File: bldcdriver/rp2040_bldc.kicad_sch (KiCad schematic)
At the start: 12 parts, among them U2 RP2040

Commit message: Added the QSPI chip but not fully interfaced with the button/jumper, added decoupling capacitors for the RP2040
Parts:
- added C18: 100n, symbol Device:C_Small
- added U3: W25Q128JVS, Package_SO:SOIC-8_5.23x5.23mm_P1.27mm, symbol Memory_Flash:W25Q128JVS
- U2: footprint RP2040_minimal:RP2040-QFN-56 -> RP2040:RP2040-QFN-56
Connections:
- net +3.3V: now also C18.1, U3.8 (VCC)
- net GND: now also C18.2, U3.4 (GND)
- net QSPI_SD3: now reaches U2.51 (QSPI_SD3)
- net QSPI_SD3: now also U3.7 (IO3)
- net QSPI_SCLK: now reaches U2.52 (QSPI_SCLK)
- net QSPI_SCLK: now also U3.6 (CLK)
- net QSPI_SD0: now reaches U2.53 (QSPI_SD0)
- net QSPI_SD0: now also U3.5 (DI(IO0))
- net QSPI_SD2: now reaches U2.54 (QSPI_SD2)
- net QSPI_SD2: now also U3.3 (IO2)
- net QSPI_SD1: now reaches U2.55 (QSPI_SD1)
- net QSPI_SD1: now also U3.2 (DO(IO1))
- net QSPI_SS: now reaches U2.56 (QSPI_SS)
- net QSPI_SS: now also U3.1 (~{CS})

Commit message: Added a USB C Connector and wired it up to act as USB 2.0
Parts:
- added R6, R7: R_Small, symbol Device:R_Small
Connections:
- net at U2.46 (USB_DM): now also R7.2
- net at U2.47 (USB_DP): now also R6.1
- new net D+: R6.2
- new net D-: R7.1
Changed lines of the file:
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@@
+	(wire
+		(pts
+			(xy 162.56 67.31) (xy 166.37 67.31)
+		)
+		(stroke
+			(width 0)
+			(type default)
+		)
+	)
 	(wire
 		(pts
@@
 	(wire
 		(pts
+			(xy 162.56 69.85) (xy 166.37 69.85)
+		)
+		(stroke
+			(width 0)
+			(type default)
+		)
+	)
+	(wire
+		(pts
 			(xy 151.13 45.72) (xy 160.02 45.72)
 		)
@@
 	(wire
 		(pts
+			(xy 171.45 69.85) (xy 176.53 69.85)
+		)
+		(stroke
+			(width 0)
+			(type default)
+		)
+	)
+	(wire
+		(pts
 			(xy 39.37 119.38) (xy 50.8 119.38)
 		)
@@
 		(pts
 			(xy 118.11 161.29) (xy 118.11 166.37)
+		)
+		(stroke
+			(width 0)
+			(type default)
+		)
+	)
+	(wire
+		(pts
+			(xy 171.45 67.31) (xy 176.53 67.31)
 		)
 		(stroke
@@
 		)
 	)
-	(label "QSPI_SD1"
-		(at 87.63 85.09 0)
+	(label "D-"
+		(at 176.53 69.85 0)
 		(fields_autoplaced yes)
 		(effects
@@
 		)
 	)
-	(label "QSPI_SD2"
-		(at 87.63 87.63 0)
+	(label "QSPI_SD1"
+		(at 87.63 85.09 0)
 		(fields_autoplaced yes)
 		(effects
@@
 		)
 	)
-	(label "QSPI_SD1"
-		(at 39.37 124.46 0)
+	(label "QSPI_SD2"
+		(at 87.63 87.63 0)
 		(fields_autoplaced yes)
 		(effects
@@
 		)
 	)
-	(label "QSPI_SD0"
-		(at 39.37 121.92 0)
+	(label "QSPI_SD1"
+		(at 39.37 124.46 0)
 		(fields_autoplaced yes)
 		(effects
@@
 		)
 	)
-	(label "QSPI_SS"
-		(at 87.63 78.74 0)
+	(label "QSPI_SD0"
+		(at 39.37 121.92 0)
 		(fields_autoplaced yes)
 		(effects
@@
 		)
 	)
-	(label "QSPI_SCLK"
-		(at 87.63 93.98 0)
+	(label "QSPI_SS"
+		(at 87.63 78.74 0)
 		(fields_autoplaced yes)
 		(effects
@@
 	)
 	(label "QSPI_SCLK"
+		(at 87.63 93.98 0)
+		(fields_autoplaced yes)
+		(effects
+			(font
+				(size 1.27 1.27)
+			)
+			(justify left bottom)
+		)
+	)
+	(label "QSPI_SCLK"
 		(at 39.37 119.38 0)
+		(fields_autoplaced yes)
+		(effects
+			(font
+				(size 1.27 1.27)
+			)
+			(justify left bottom)
+		)
+	)
+	(label "D+"
+		(at 176.53 67.31 0)
 		(fields_autoplaced yes)
 		(effects
@@
 	)
 	(symbol
+		(lib_id "Device:R_Small")
+		(at 168.91 67.31 90)
+		(unit 1)
+		(exclude_from_sim no)
+		(in_bom yes)
+		(on_board yes)
+		(dnp no)
+		(fields_autoplaced yes)
+		(property "Reference" "R6"
+			(at 168.91 62.23 90)
+			(effects
+				(font
+					(size 1.27 1.27)
+				)
+			)
+		)
+		(property "Value" "R_Small"
+			(at 168.91 64.77 90)
+			(effects
+				(font
+					(size 1.27 1.27)
+				)
+			)
+		)
+		(property "Footprint" ""
+			(at 168.91 67.31 0)
+			(effects
+				(font
+					(size 1.27 1.27)
+				)
+				(hide yes)
+			)
+		)
+		(property "Datasheet" "~"
+			(at 168.91 67.31 0)
+			(effects
+				(font
+					(size 1.27 1.27)
+				)
+				(hide yes)
+			)
+		)
+		(property "Description" "Resistor, small symbol"
+			(at 168.91 67.31 0)
+			(effects
+				(font
+					(size 1.27 1.27)
+				)
+				(hide yes)
+			)
+		)
+		(pin "1"
+		)
+		(pin "2"
+		)
+		(instances
+			(project ""
+				(path "/386247e7-fbba-4db7-978d-7d877f3805e6/bfcb2737-5ae5-450f-a29a-35bd17b628aa"
+					(reference "R6")
+					(unit 1)
+				)
+			)
+		)
+	)
+	(symbol
 		(lib_id "power:GND")
 		(at 66.04 110.49 0)
@@
 					(unit 1)
 				)
+			)
+		)
+	)
+	(symbol
+		(lib_id "Device:R_Small")
+		(at 168.91 69.85 270)
+		(unit 1)
+		(exclude_from_sim no)
+		(in_bom yes)
+		(on_board yes)
+		(dnp no)
+		(property "Reference" "R7"
+			(at 168.91 72.39 90)
+			(effects
+				(font
+					(size 1.27 1.27)
+				)
+			)
+		)
+		(property "Value" "R_Small"
+			(at 168.91 74.93 90)
+			(effects
+				(font
+					(size 1.27 1.27)
+				)
+			)
+		)
+		(property "Footprint" ""
+			(at 168.91 69.85 0)
+			(effects
+				(font
+					(size 1.27 1.27)
+				)
+				(hide yes)
+			)
+		)
+		(property "Datasheet" "~"
+			(at 168.91 69.85 0)
+			(effects
+				(font
+					(size 1.27 1.27)
+				)
+				(hide yes)
+			)
+		)
+		(property "Description" "Resistor, small symbol"
+			(at 168.91 69.85 0)
+			(effects
+				(font
+					(size 1.27 1.27)
+				)
+				(hide yes)
+			)
+		)
+		(pin "1"
+		)
+		(pin "2"
+		)
+		(instances
+			(project "bldcdriver"
+				(path "/386247e7-fbba-4db7-978d-7d877f3805e6/bfcb2737-5ae5-450f-a29a-35bd17b628aa"
+					(reference "R7")
+					(unit 1)
+				)

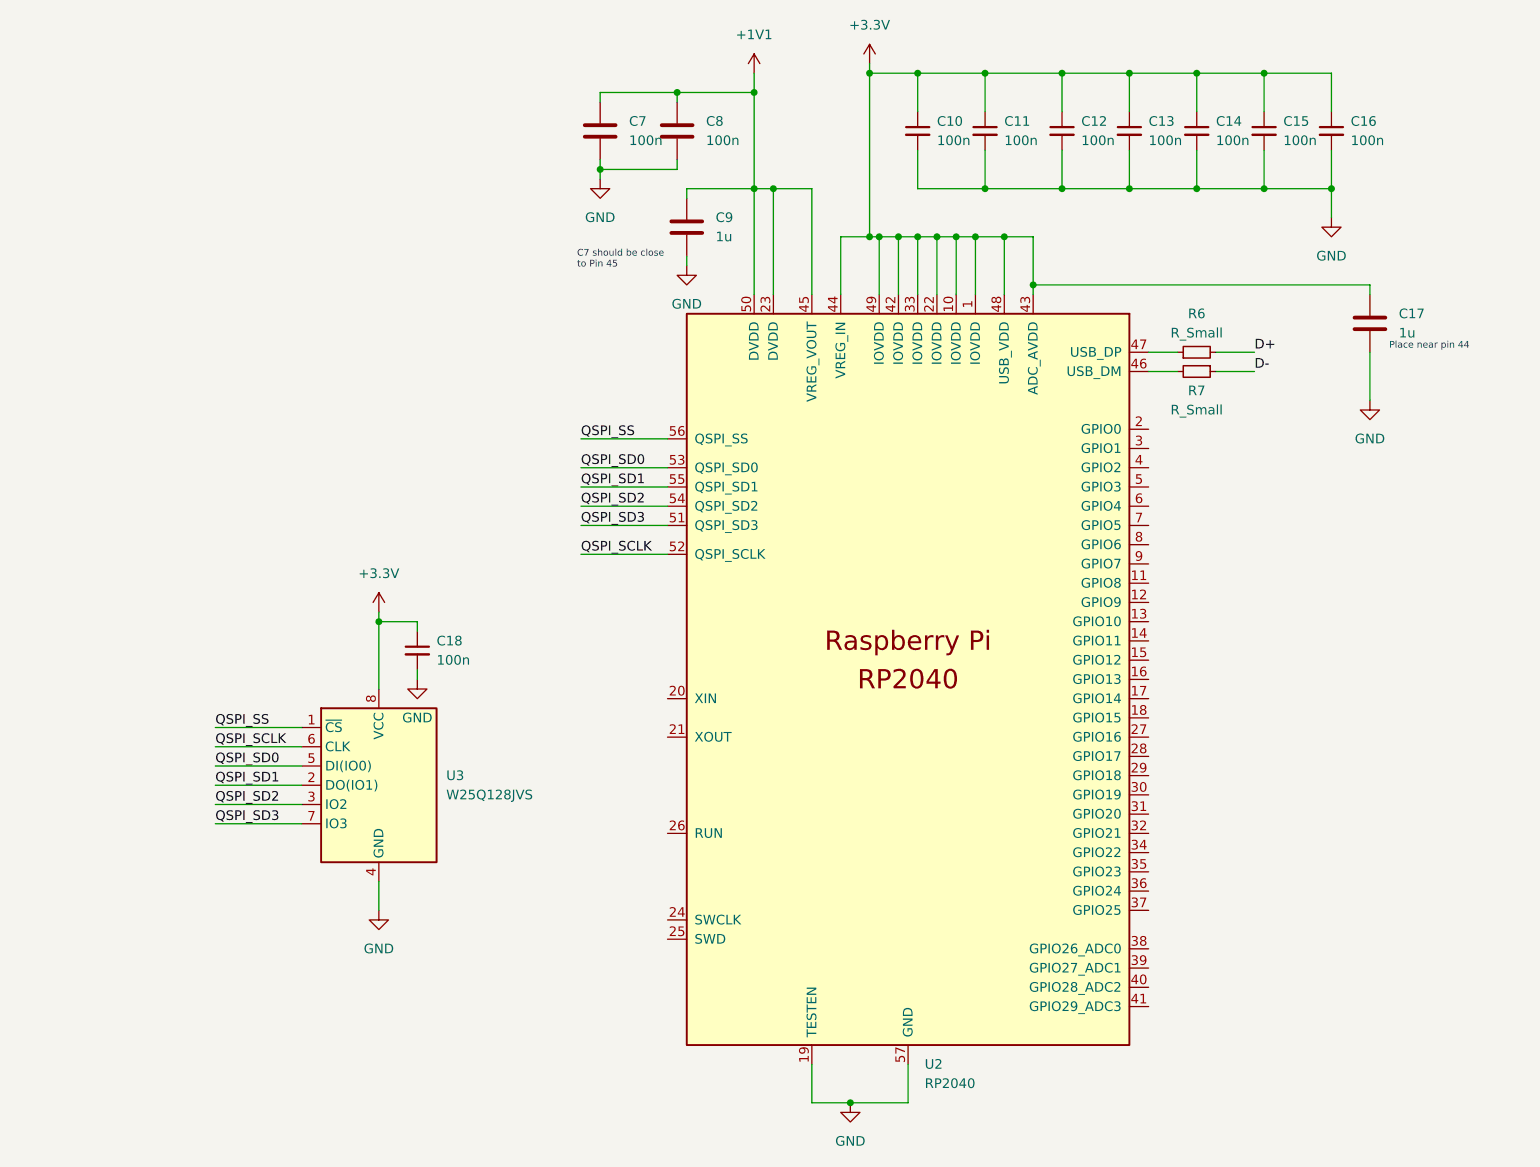
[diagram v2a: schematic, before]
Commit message: Finished DRV side fully, RP2040 almost fully done, FOC sensorless and sensor parts and power parts are left
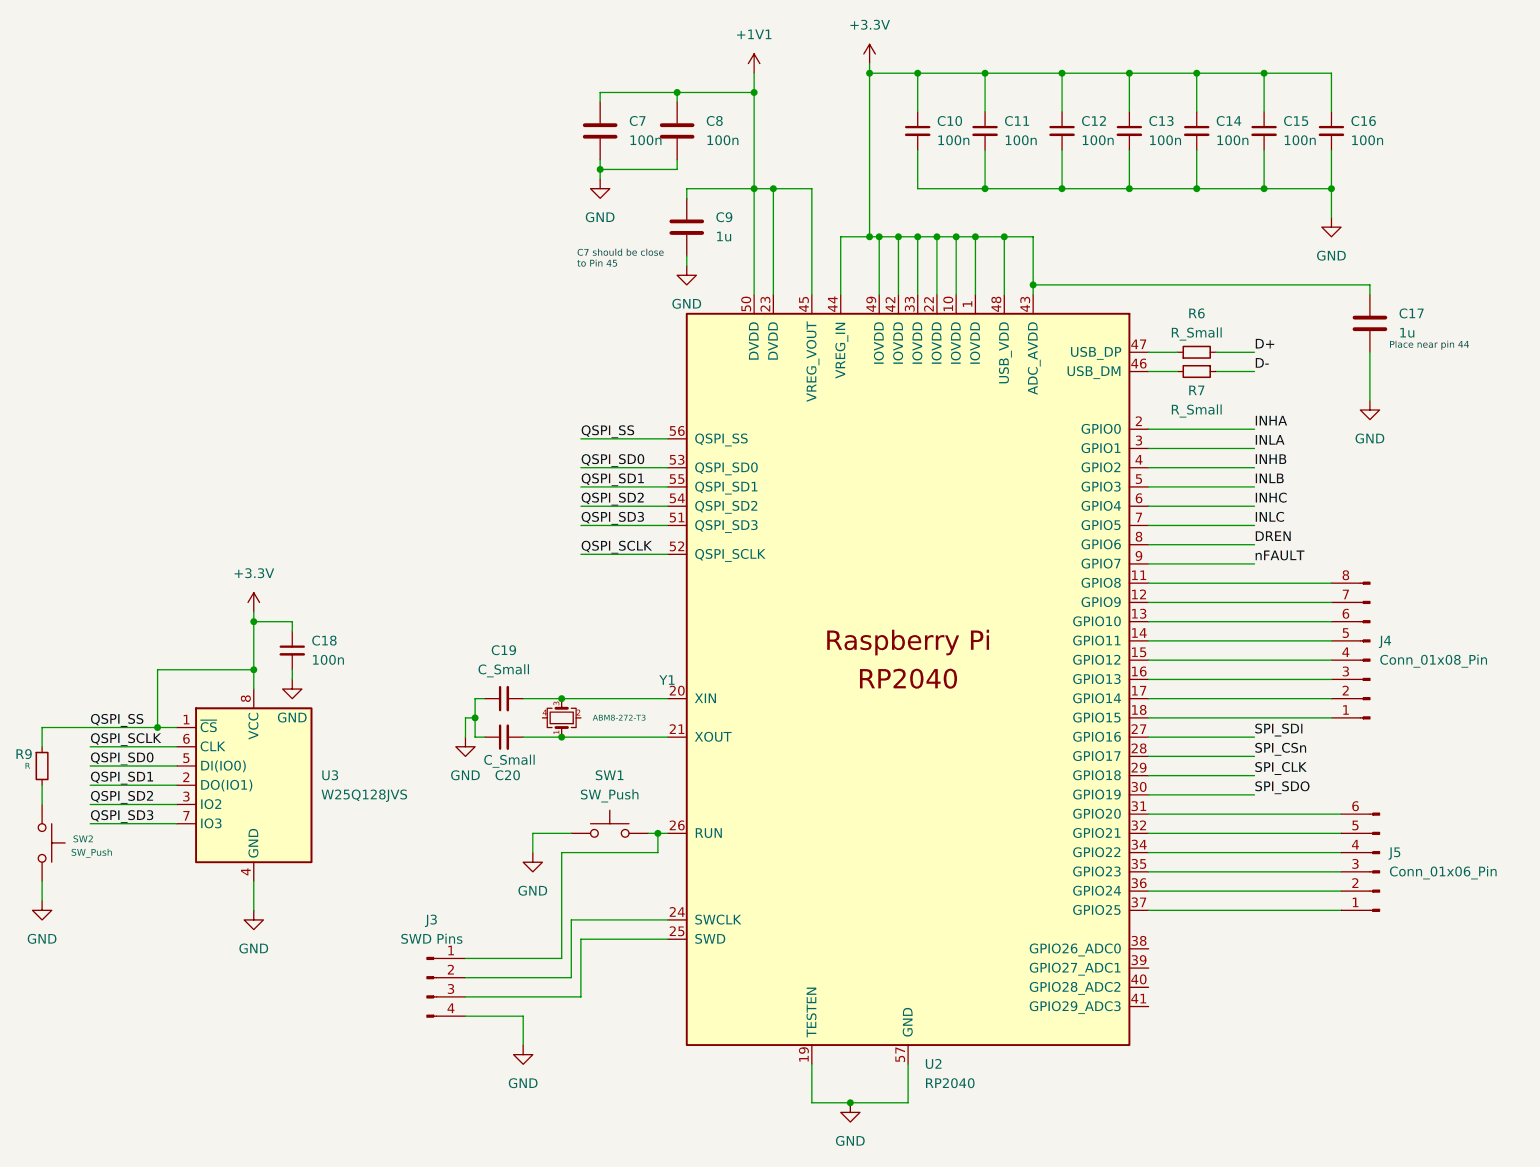
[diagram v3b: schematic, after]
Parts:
- added C19, C20: C_Small, symbol Device:C_Small
- added J3: SWD Pins, symbol Connector:Conn_01x04_Pin
- added J4: Conn_01x08_Pin, symbol Connector:Conn_01x08_Pin
- added J5: Conn_01x06_Pin, symbol Connector:Conn_01x06_Pin
- added R9: R, symbol Device:R_Small
- added SW1, SW2: SW_Push, Button_Switch_THT:SW_PUSH_6mm, symbol Switch:SW_Push
- added Y1: ABM8-272-T3, symbol Device:Crystal_GND24_Small
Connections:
- net QSPI_SS is gone; now on net +3.3V: U2.56 (QSPI_SS), U3.1 (~{CS})
- net +3.3V: now also R9.1
- net GND: now also C19.1, C20.1, J3.4 (Pin_4), SW1.1, SW2.2
- net at U2.11 (GPIO8): now also J4.8 (Pin_8)
- net at U2.12 (GPIO9): now also J4.7 (Pin_7)
- net at U2.13 (GPIO10): now also J4.6 (Pin_6)
- net at U2.14 (GPIO11): now also J4.5 (Pin_5)
- net at U2.15 (GPIO12): now also J4.4 (Pin_4)
- net at U2.16 (GPIO13): now also J4.3 (Pin_3)
- net at U2.17 (GPIO14): now also J4.2 (Pin_2)
- net at U2.18 (GPIO15): now also J4.1 (Pin_1)
- net INHA: now reaches U2.2 (GPIO0)
- net at U2.20 (XIN): now also C19.2, Y1.3
- net at U2.21 (XOUT): now also C20.2, Y1.1
- net at U2.24 (SWCLK): now also J3.2 (Pin_2)
- net at U2.25 (SWD): now also J3.3 (Pin_3)
- net at U2.26 (RUN): now also J3.1 (Pin_1), SW1.2
- net SPI_SDI: now reaches U2.27 (GPIO16)
- net SPI_CSn: now reaches U2.28 (GPIO17)
- net SPI_CLK: now reaches U2.29 (GPIO18)
- net INLA: now reaches U2.3 (GPIO1)
- net SPI_SDO: now reaches U2.30 (GPIO19)
- net at U2.31 (GPIO20): now also J5.6 (Pin_6)
- net at U2.32 (GPIO21): now also J5.5 (Pin_5)
- net at U2.34 (GPIO22): now also J5.4 (Pin_4)
- net at U2.35 (GPIO23): now also J5.3 (Pin_3)
- net at U2.36 (GPIO24): now also J5.2 (Pin_2)
- net at U2.37 (GPIO25): now also J5.1 (Pin_1)
- net INHB: now reaches U2.4 (GPIO2)
- net INLB: now reaches U2.5 (GPIO3)
- net INHC: now reaches U2.6 (GPIO4)
- net INLC: now reaches U2.7 (GPIO5)
- net DREN: now reaches U2.8 (GPIO6)
- net nFAULT: now reaches U2.9 (GPIO7)
- new net: R9.2, SW2.1
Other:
- moved on the sheet: C18, U3
